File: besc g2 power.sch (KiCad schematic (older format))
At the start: 167 parts, among them Q1 Q_NMOS_DGS, Q10 Q_NMOS_DGS, Q11 Q_NMOS_DGS, Q12 Q_NMOS_DGS, Q13 Q_NMOS_DGS, Q14 Q_NMOS_DGS, Q15 Q_NMOS_DGS, Q16 Q_NMOS_DGS, Q17 Q_NMOS_DGS, Q18 Q_NMOS_DGS, Q19 Q_NMOS_DGS, Q2 Q_NMOS_DGS, Q20 Q_NMOS_DGS, Q21 Q_NMOS_DGS, Q22 Q_NMOS_DGS, Q23 Q_NMOS_DGS, Q24 Q_NMOS_DGS, Q3 Q_NMOS_DGS, Q4 Q_NMOS_DGS, Q5 Q_NMOS_DGS, Q6 Q_NMOS_DGS, Q7 Q_NMOS_DGS, Q8 Q_NMOS_DGS, Q9 Q_NMOS_DGS, U1 INA240A1D, U2 INA240A1D, U3 INA240A1D

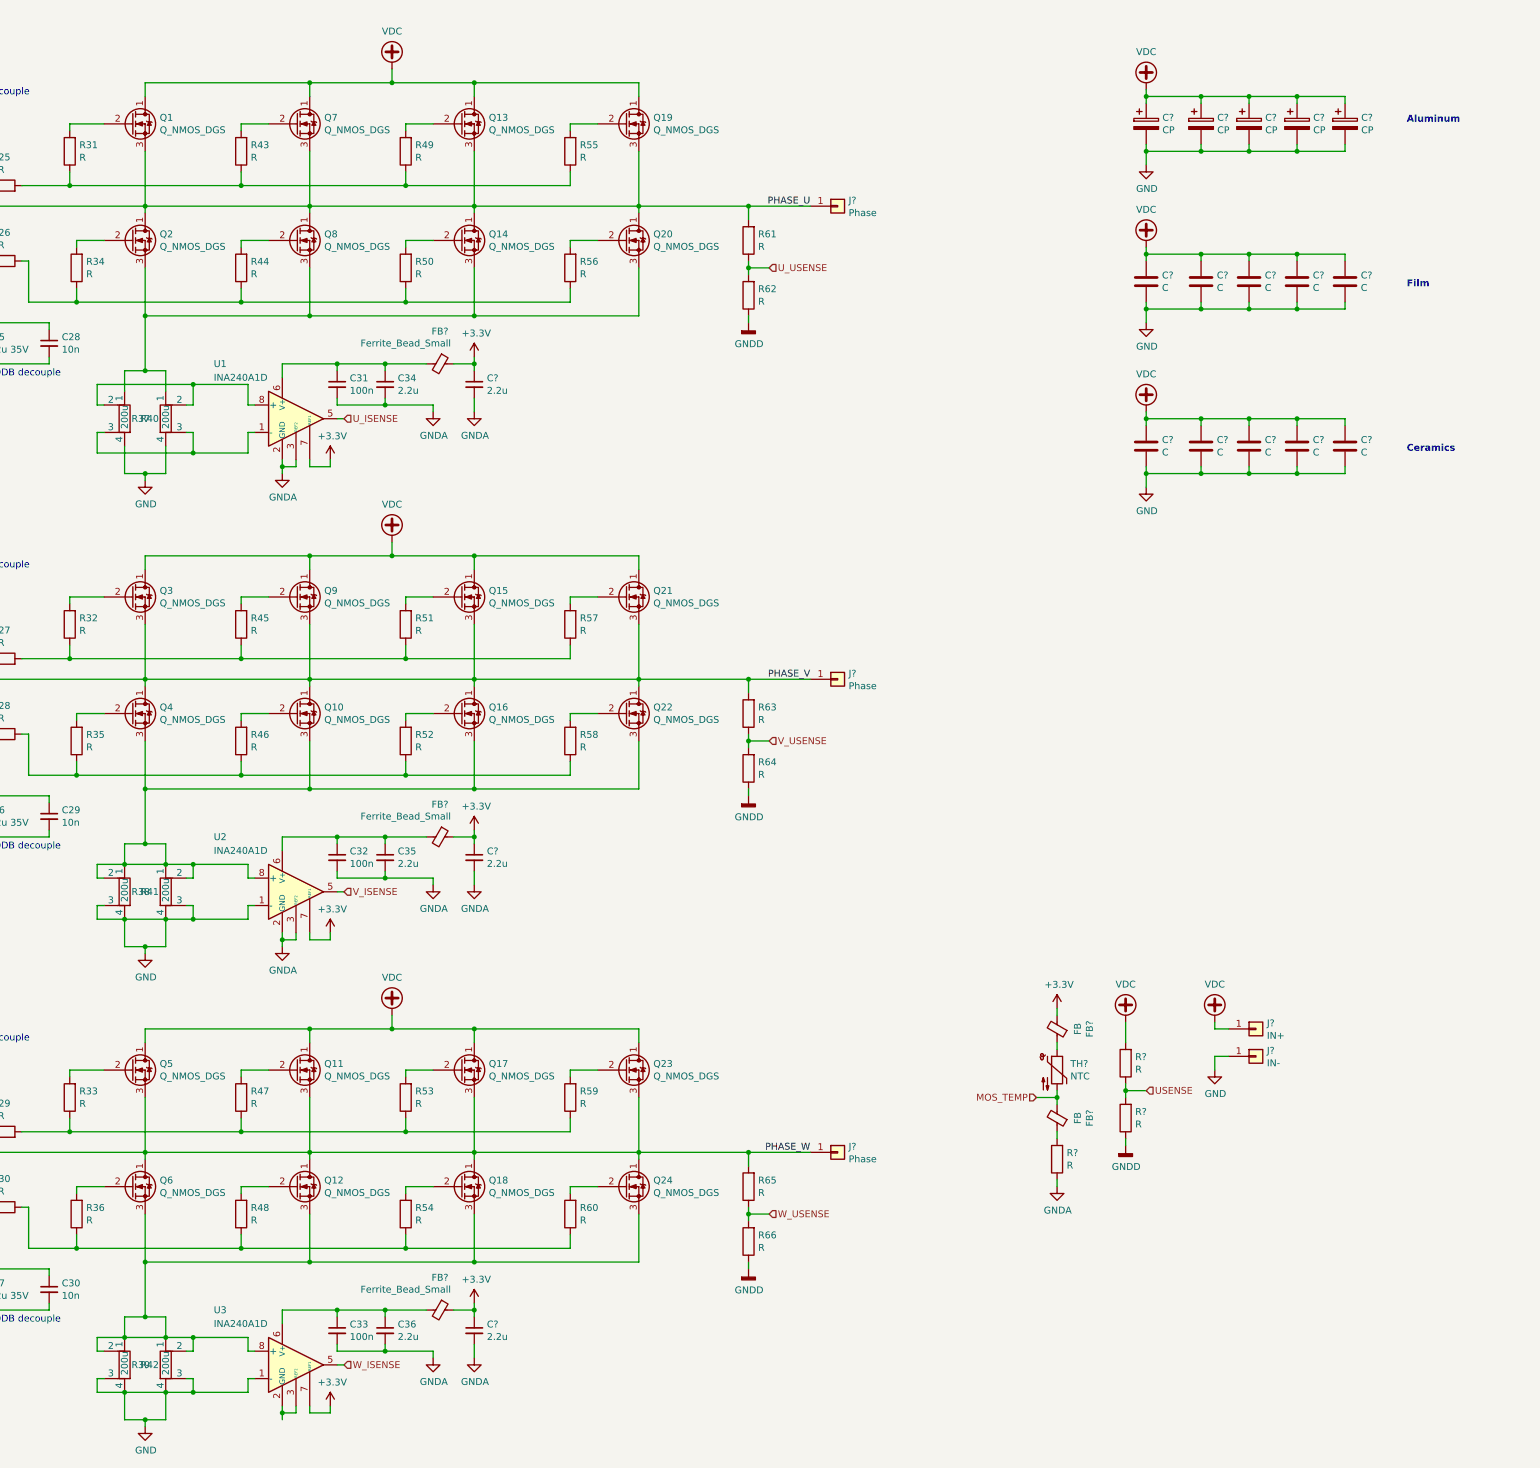
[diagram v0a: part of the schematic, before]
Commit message: power stage layout draft
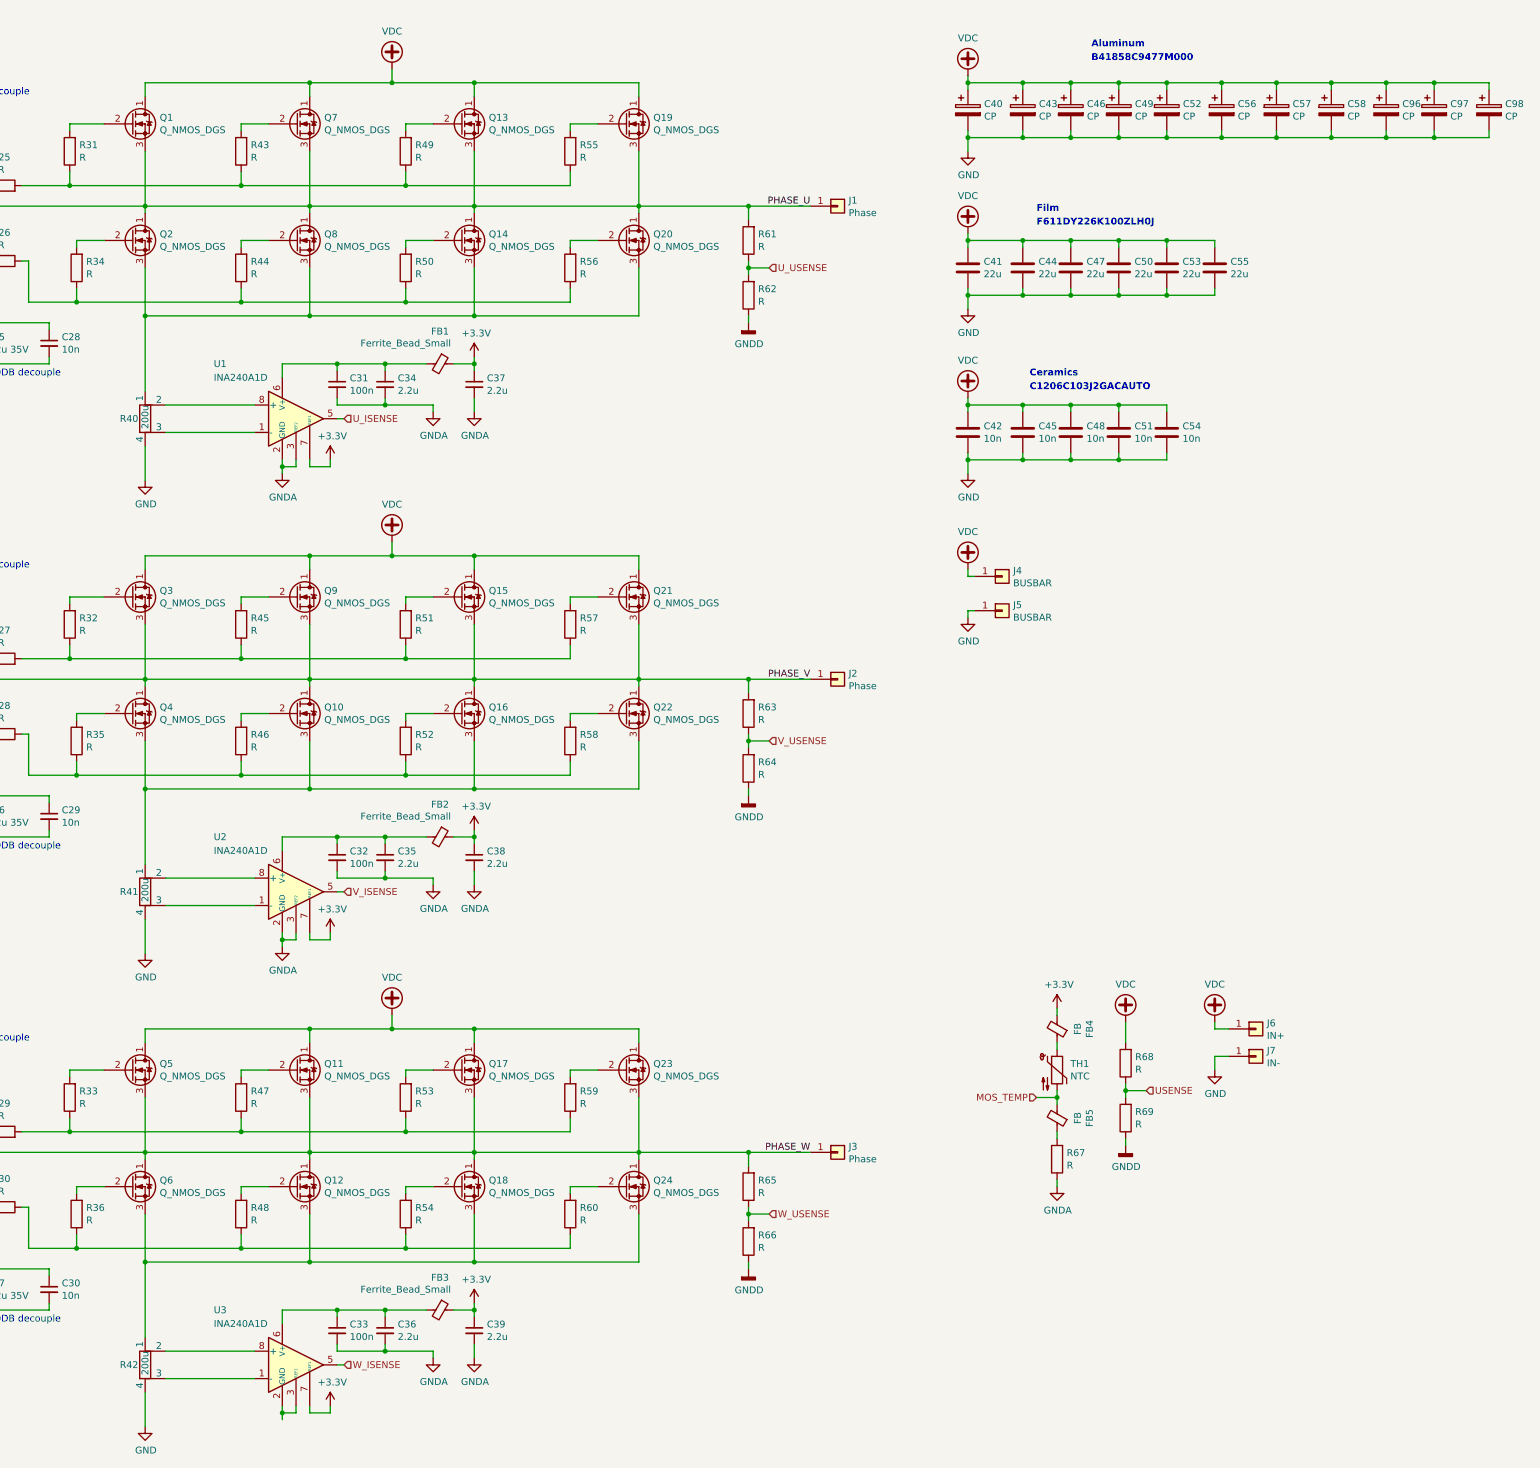
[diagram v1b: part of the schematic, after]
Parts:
- removed C? (x2): C, symbol Device:C
- removed R37, R38, R39: 200u, Resistor_SMD:R_Shunt_Vishay_WSK2512_6332Metric_T1.19mm, symbol Device:R_Shunt
- added C50, C53, C55: 22u, Capacitor_THT:C_Rect_L18.0mm_W11.0mm_P15.00mm_FKS3_FKP3, symbol Device:C
- added C56, C57, C58, C96, C97, C98: CP, Capacitor_THT:C_Radial_D18.0mm_H35.5mm_P7.50mm, symbol Device:CP
- added J4, J5: BUSBAR, moje:busbar1, symbol Connector_Generic:Conn_01x01
- C40, C43, C46, C49, C52: renamed from C?; footprint (none) -> Capacitor_THT:C_Radial_D18.0mm_H35.5mm_P7.50mm
- C41, C44, C47: renamed from C?; value C -> 22u; footprint (none) -> Capacitor_THT:C_Rect_L18.0mm_W11.0mm_P15.00mm_FKS3_FKP3
- C42, C45, C48, C51, C54: renamed from C?; value C -> 10n; footprint (none) -> Capacitor_SMD:C_1206_3216Metric
- DRV1, DRV2, DRV3: footprint Package_SO:SOIC-16_4.55x10.3mm_P1.27mm -> Package_SO:SOIC-16_3.9x9.9mm_P1.27mm
- FB1, FB2, FB3, FB4, FB5: renamed from FB?; footprint (none) -> Inductor_SMD:L_0603_1608Metric
- J1, J2, J3, J6, J7: renamed from J?; footprint (none) -> moje:8awg_wirepad
- Q1, Q10, Q11, Q12, Q13, Q14, Q15, Q16, Q17, Q18, Q19, Q2, Q20, Q21, Q22, Q23, Q24, Q3, Q4, Q5, Q6, Q7, Q8, Q9: footprint Package_TO_SOT_THT:TO-220-3_Vertical -> Package_TO_SOT_THT:TO-220-3_Horizontal_TabUp
- R40, R41, R42: footprint Resistor_SMD:R_Shunt_Vishay_WSK2512_6332Metric_T1.19mm -> moje:LRMAP5930x
- TH1: renamed from TH?; footprint (none) -> Resistor_SMD:R_0603_1608Metric
- gave numbers to parts that had none: 6
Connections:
- wire segments 669 -> 627
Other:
- note added: "B41858C9477M000"
- note added: "C1206C103J2GACAUTO"
- note added: "F611DY226K100ZLH0J"
- moved on the sheet: C40, C41, C42, C43, C44, C45, C46, C47, C48, C49, C51, C52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

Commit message: isolated drivers, layout
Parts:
- removed C7: 10n, Capacitor_SMD:C_0603_1608Metric, symbol Device:C_Small
- removed DRV1, DRV2, DRV3: UCC21222, Package_SO:SOIC-16_3.9x9.9mm_P1.27mm, symbol moje:UCC21222
- removed R13: R, Resistor_SMD:R_0603_1608Metric, symbol Device:R
- removed R25, R26, R27, R28, R29, R30: R, Resistor_SMD:R_0805_2012Metric, symbol Device:R
- added C1: 2.2u 35V, Capacitor_SMD:C_1206_3216Metric, symbol Device:C_Small
- added R19: R, Resistor_SMD:R_0603_1608Metric, symbol Device:R
- added U1, U2, U3: UCC21520DW, Package_SO:SOIC-16W_7.5x10.3mm_P1.27mm, symbol Driver_FET:UCC21520DW
- C10, C11, C12: value 10n -> 100n; footprint Capacitor_SMD:C_0603_1608Metric -> Capacitor_SMD:C_0805_2012Metric
- C13, C14, C15: value 220n -> 10n
- C16, C17, C18: value 2.2u 35V -> 100n
- C2, C3: value 10n -> 2.2u 35V; footprint Capacitor_SMD:C_0603_1608Metric -> Capacitor_SMD:C_1206_3216Metric
- C23, C24: value 10n -> 2.2u 35V; footprint Capacitor_SMD:C_0805_2012Metric -> Capacitor_SMD:C_1206_3216Metric
- C26, C27: value 2.2u 35V -> 10n; footprint Capacitor_SMD:C_1206_3216Metric -> Capacitor_SMD:C_0805_2012Metric
- Q1, Q10, Q11, Q12, Q13, Q14, Q15, Q16, Q17, Q18, Q19, Q2, Q20, Q21, Q22, Q23, Q24, Q3, Q4, Q5, Q6, Q7, Q8, Q9: footprint Package_TO_SOT_THT:TO-220-3_Horizontal_TabUp -> moje:TO-220-3_hor_tabup; symbol Device:Q_NMOS_DGS -> Device:Q_NMOS_GDS
- R11, R12: value R -> 2.2; footprint Resistor_SMD:R_0603_1608Metric -> Resistor_SMD:R_1206_3216Metric
- R17, R18: value 2.2 -> R; footprint Resistor_SMD:R_1206_3216Metric -> Resistor_SMD:R_0603_1608Metric
- R25: renamed from R31; value R -> 10
- R26: renamed from R32; value R -> 10
- R27: renamed from R33; value R -> 10
- R28: renamed from R34; value R -> 10
- R29: renamed from R35; value R -> 10
- R30: renamed from R36; value R -> 10
- R34: renamed from R43; value R -> 10
- R35: renamed from R44; value R -> 10
- R36: renamed from R45; value R -> 10
- R37: renamed from R46; value R -> 10
- R38: renamed from R47; value R -> 10
- R39: renamed from R48; value R -> 10
- R40: renamed from R49; value R -> 10
- R41: renamed from R50; value R -> 10
- R42: renamed from R51; value R -> 10
- R43: renamed from R52; value R -> 10
- R44: renamed from R53; value R -> 10
- R45: renamed from R54; value R -> 10
- R46: renamed from R55; value R -> 10
- R47: renamed from R56; value R -> 10
- R48: renamed from R57; value R -> 10
- R49: renamed from R58; value R -> 10
- R50: renamed from R59; value R -> 10
- R51: renamed from R60; value R -> 10
- renumbered C25 to C22, C22 to C25, C1 to C4, C96 to C59, C97 to C60, C98 to C61, C4 to C7, R16 to R10, R10 to R13, R19 to R16, R40 to R31, R41 to R32, R42 to R33, R61 to R52, R62 to R53, R63 to R54, R64 to R55, R65 to R56, R66 to R57, R67 to R58, R68 to R59, R69 to R60, U1 to U4, U2 to U5, U3 to U6
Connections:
- net labels added: GND_U, GND_V, GND_W
- wire segments 627 -> 624
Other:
- note added: "F611BY685K100A"
- note added: "HIGH SIDE\nsupply & decouple"
- note added: "LOW SIDE decouple"
- note removed: "F611DY226K100ZLH0J"
- note removed: "VDDA supply & decouple"
- note removed: "VDDB decouple"
- moved on the sheet: C19, C22, C25, C28, C4, C7, D1, R1, R10, R13, R16, R2

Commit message: 12V PS, isolated gate drivers
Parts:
- C1: renamed from C19; value 2.2u 35V -> 4.7u 25V
- C23: renamed from C16; footprint Capacitor_SMD:C_0805_2012Metric -> Capacitor_SMD:C_0603_1608Metric
- C36: renamed from C20; value 2.2u 35V -> 4.7u 25V
- C41: renamed from C17; footprint Capacitor_SMD:C_0805_2012Metric -> Capacitor_SMD:C_0603_1608Metric
- C44: renamed from C23; value 2.2u 35V -> 4.7u 25V
- C49: renamed from C21; value 2.2u 35V -> 4.7u 25V
- C54: renamed from C18; footprint Capacitor_SMD:C_0805_2012Metric -> Capacitor_SMD:C_0603_1608Metric
- C57: renamed from C24; value 2.2u 35V -> 4.7u 25V
- R10: renamed from R52; footprint Resistor_SMD:R_1210_3225Metric -> Resistor_SMD:R_0805_2012Metric
- R29: renamed from R54; footprint Resistor_SMD:R_1210_3225Metric -> Resistor_SMD:R_0805_2012Metric
- R51: renamed from R56; footprint Resistor_SMD:R_1210_3225Metric -> Resistor_SMD:R_0805_2012Metric
- renumbered C58 to C10, C59 to C11, C60 to C12, C61 to C13, C4 to C14, C7 to C15, C13 to C16, C41 to C17, C44 to C18, C47 to C19, C25 to C2, C50 to C20, C53 to C21, C55 to C22, C1 to C24, C10 to C25, C22 to C26, C28 to C27, C31 to C28, C34 to C29, C40 to C3, C37 to C30, C42 to C31, C45 to C32, C48 to C33, C51 to C34, C54 to C35, C26 to C37, C5 to C38, C8 to C39, C43 to C4, C14 to C40, C2 to C42, C11 to C43, C29 to C45, C32 to C46, C35 to C47, C38 to C48, C46 to C5, C27 to C50, C6 to C51, C9 to C52, C15 to C53, C3 to C55, C12 to C56, C30 to C58, C33 to C59, C49 to C6, C36 to C60, C39 to C61, C52 to C7, C56 to C8, C57 to C9, FB4 to FB3, FB5 to FB4, FB3 to FB5, J4 to J2, J5 to J3, J2 to J4, J6 to J5, J7 to J6, J3 to J7, Q9 to Q10, Q15 to Q11, Q21 to Q12, Q4 to Q13, Q10 to Q14, Q16 to Q15, Q22 to Q16, Q5 to Q17, Q11 to Q18, Q17 to Q19, Q7 to Q2, Q23 to Q20, Q6 to Q21, Q12 to Q22, Q18 to Q23, Q13 to Q3, Q19 to Q4, Q2 to Q5, Q8 to Q6, Q14 to Q7, Q20 to Q8, Q3 to Q9, R10 to R1, R2 to R11, R28 to R12, R35 to R13, R41 to R14, R47 to R15, R3 to R16, R53 to R17, R19 to R18, R31 to R19, R25 to R2, R11 to R20, R26 to R21, R36 to R22, R42 to R23, R48 to R24, R14 to R25, R17 to R26, R23 to R27, R4 to R28, R34 to R3, R5 to R30, R29 to R31, R37 to R32, R43 to R33, R49 to R34, R6 to R35, R55 to R36, R20 to R37, R32 to R38, R12 to R39, R40 to R4, R59 to R40, R27 to R41, R38 to R42, R44 to R43, R50 to R44, R60 to R45, R15 to R46, R18 to R47, R24 to R48, R58 to R49, R46 to R5, R7 to R50, R8 to R52, R30 to R53, R39 to R54, R45 to R55, R51 to R56, R9 to R57, R57 to R58, R21 to R59, R13 to R6, R33 to R60, R16 to R7, R22 to R8, R1 to R9, U4 to U2, U2 to U3, U5 to U4, U3 to U5

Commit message: layout and routing progress
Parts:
- removed C35: 10n, Capacitor_SMD:C_1206_3216Metric, symbol Device:C
- removed FB3, FB4: FB, Inductor_SMD:L_0603_1608Metric, symbol Device:Ferrite_Bead_Small
- added C54: 2.2u, Capacitor_SMD:C_0603_1608Metric, symbol Device:C_Small
- added R58, R59, R61, R62: 1R, Resistor_SMD:R_1206_3216Metric, symbol Device:R
- C40: renamed from C3; value CP -> B41858C9477M000
- C41: renamed from C17; value 22u -> F611BY685K100A
- C42: renamed from C31; value 10n -> C1206C105K1RACTU
- C43: renamed from C4; value CP -> B41858C9477M000
- C44: renamed from C18; value 22u -> F611BY685K100A
- C45: renamed from C32; value 10n -> C1206C105K1RACTU
- C46: renamed from C5; value CP -> B41858C9477M000
- C47: renamed from C19; value 22u -> F611BY685K100A
- C48: renamed from C33; value 10n -> C1206C105K1RACTU
- C49: renamed from C6; value CP -> B41858C9477M000
- C50: renamed from C20; value 22u -> F611BY685K100A
- C51: renamed from C34; value 10n -> C1206C105K1RACTU
- C52: renamed from C7; value CP -> B41858C9477M000
- C53: renamed from C21; value 22u -> F611BY685K100A
- C55: renamed from C22; value 22u -> F611BY685K100A
- C56: renamed from C8; value CP -> B41858C9477M000
- C57: renamed from C9; value CP -> B41858C9477M000
- C58: renamed from C10; value CP -> B41858C9477M000
- C59: renamed from C11; value CP -> B41858C9477M000
- C60: renamed from C12; value CP -> B41858C9477M000
- C61: renamed from C13; value CP -> B41858C9477M000
- R52: renamed from R10; value R -> 150k
- R53: renamed from R17; value R -> 3k24
- R54: renamed from R29; value R -> 150k
- R55: renamed from R36; value R -> 3k24
- R56: renamed from R51; value R -> 150k
- R57: renamed from R58; value R -> 3k24
- R60: renamed from R49; value R -> 10k; footprint Resistor_SMD:R_0805_2012Metric -> Resistor_SMD:R_0603_1608Metric
- R63: renamed from R40; value R -> 150k; footprint Resistor_SMD:R_1210_3225Metric -> Resistor_SMD:R_0805_2012Metric
- R64: renamed from R45; value R -> 3k24
- TH1: value NTC -> 10k
- renumbered C24 to C1, C25 to C10, C43 to C11, C56 to C12, C16 to C13, C40 to C14, C53 to C15, C23 to C16, C41 to C17, C54 to C18, C1 to C19, C42 to C2, C36 to C20, C49 to C21, C26 to C22, C44 to C23, C57 to C24, C2 to C25, C37 to C26, C50 to C27, C27 to C28, C45 to C29, C55 to C3, C58 to C30, C28 to C31, C46 to C32, C59 to C33, C29 to C34, C47 to C35, C60 to C36, C30 to C37, C48 to C38, C61 to C39, C14 to C4, C38 to C5, C51 to C6, C15 to C7, C39 to C8, C52 to C9, FB5 to FB3, J4 to J2, J7 to J3, J2 to J4, J3 to J5, J5 to J6, J6 to J7, Q14 to Q10, Q18 to Q11, Q22 to Q12, Q3 to Q13, Q7 to Q14, Q11 to Q15, Q15 to Q16, Q19 to Q17, Q23 to Q18, Q4 to Q19, Q5 to Q2, Q8 to Q20, Q12 to Q21, Q16 to Q22, Q20 to Q23, Q9 to Q3, Q13 to Q4, Q17 to Q5, Q21 to Q6, Q2 to Q7, Q6 to Q8, Q10 to Q9, R9 to R1, R1 to R10, R20 to R11, R39 to R12, R6 to R13, R25 to R14, R46 to R15, R7 to R16, R26 to R17, R47 to R18, R18 to R19, R11 to R2, R37 to R20, R59 to R21, R8 to R22, R27 to R23, R48 to R24, R2 to R25, R21 to R26, R41 to R27, R12 to R28, R31 to R29, R16 to R3, R53 to R30, R19 to R31, R38 to R32, R60 to R33, R3 to R34, R13 to R35, R22 to R36, R32 to R37, R42 to R38, R54 to R39, R28 to R4, R4 to R40, R14 to R41, R23 to R42, R33 to R43, R43 to R44, R55 to R45, R5 to R46, R15 to R47, R24 to R48, R34 to R49, R30 to R5, R44 to R50, R56 to R51, R35 to R6, R50 to R7, R52 to R8, R57 to R9, U3 to U2, U5 to U3, U2 to U4, U4 to U5
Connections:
- net +3V3: now also TH1.1; no longer U4.7 (REF1), U5.7 (REF1), U6.7 (REF1)
- net GND: now also R58.1, R59.1, R61.1, R62.1; no longer C42.2, C45.2, C48.2, C51.2
- net GNDA: now also R53.1, R55.1, R57.1, R64.1, U6.2 (GND), U6.3 (REF2), U6.4 (GND), C54.2
- net GNDD: no longer R53.1, R55.1, R57.1, R64.1
- net MOS_TEMP: now also R60.2, C54.1
- net VSUPA_U: now reaches C31.1, C34.1, FB1.2, U4.6 (V+)
- net VSUPA_U: now also U4.7 (REF1)
- net VSUPA_W: now reaches C33.1, C36.1, FB3.2, U6.6 (V+)
- net VSUPA_W: now also U6.7 (REF1)
- net VSUPA_V: now reaches C32.1, C35.1, FB2.2, U5.6 (V+)
- net VSUPA_V: now also U5.7 (REF1)
- new net: C42.2, R58.2
- new net: C45.2, R59.2
- new net: C48.2, R61.2
- new net: C51.2, R62.2
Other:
- note added: "C1206C105K1RACTU"
- note added: "HF snubbers"
- note removed: "C1206C103J2GACAUTO"
- note removed: "Ceramics"
- moved on the sheet: J4, J5, J6, J7, R60

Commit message: finished routing, added bom and step
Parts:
- C1, C2, C3: footprint Capacitor_SMD:C_1206_3216Metric -> Capacitor_SMD:C_0805_2012Metric
- C10, C11, C12, C25, C26, C27, C28, C29, C30: footprint Capacitor_SMD:C_0805_2012Metric -> Capacitor_SMD:C_0603_1608Metric
- C13, C14, C15, C4, C5, C6, C7, C8, C9: value 10n -> 270p
- C22: value 2.2u 35V -> 4.7u 25V
- C43, C46, C49, C52, C56, C57, C58, C59, C60, C61: value B41858C9477M000 -> B41858C9477M000
- D1, D2, D3: value D_Schottky -> SS115+
- FB1, FB2, FB3: value Ferrite_Bead_Small -> BLM18AG102SN1D
- J1, J2, J3: value Phase -> PHASE WIRE
- Q1, Q10, Q11, Q12, Q13, Q14, Q15, Q16, Q17, Q18, Q19, Q2, Q20, Q21, Q22, Q23, Q24, Q3, Q4, Q5, Q6, Q7, Q8, Q9: value Q_NMOS_DGS -> IRF135B203
- R1, R2, R3, R4, R5, R6, R7, R8, R9: value R -> 60R4
- R10, R11, R12: value 2.2 -> 2.2R
- R13, R14, R15, R16, R17, R18, R22, R23, R24: value R -> 2k2
- R19, R20, R21: value R -> 10k
- R25, R26, R27, R28, R29, R30, R34, R35, R36, R37, R38, R39, R40, R41, R42, R43, R44, R45, R46, R47, R48, R49, R50, R51: value 10 -> 10R
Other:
- note added: "Analog ground is kept sepparate"
- note added: "Bootstrap supply for high side gates"
- note added: "Bulk capacitance to compensate battery wire impedance"
- note added: "Ceramics"
- note added: "DT=10xR\nns / kOhm"
- note added: "Each fet has its own gate resistor \nto even out switching losses"
- note added: "Ferrite bead for HF filtering"
- note added: "HF capacitance to compensate power stage impedance"
- note added: "Pulldowns to\nintroduce current\nin signal lines for\nnoise immunity"
- note added: "Refference is 3.3V / 2"
- note added: "Signal filter"
